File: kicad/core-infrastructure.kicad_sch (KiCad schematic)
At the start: 10 parts, among them J1 JST XH Balance Lead, J2 T-Connector Deans 14 AWG, J3 JST XH Balance Lead, SW2 Latching Push Button, U5 PCA9685PW, U6 JZK 2S 7.4V 8A BMS, U7 MP1584 Buck Converter 5V, U8 ESP32-S3 Super Mini

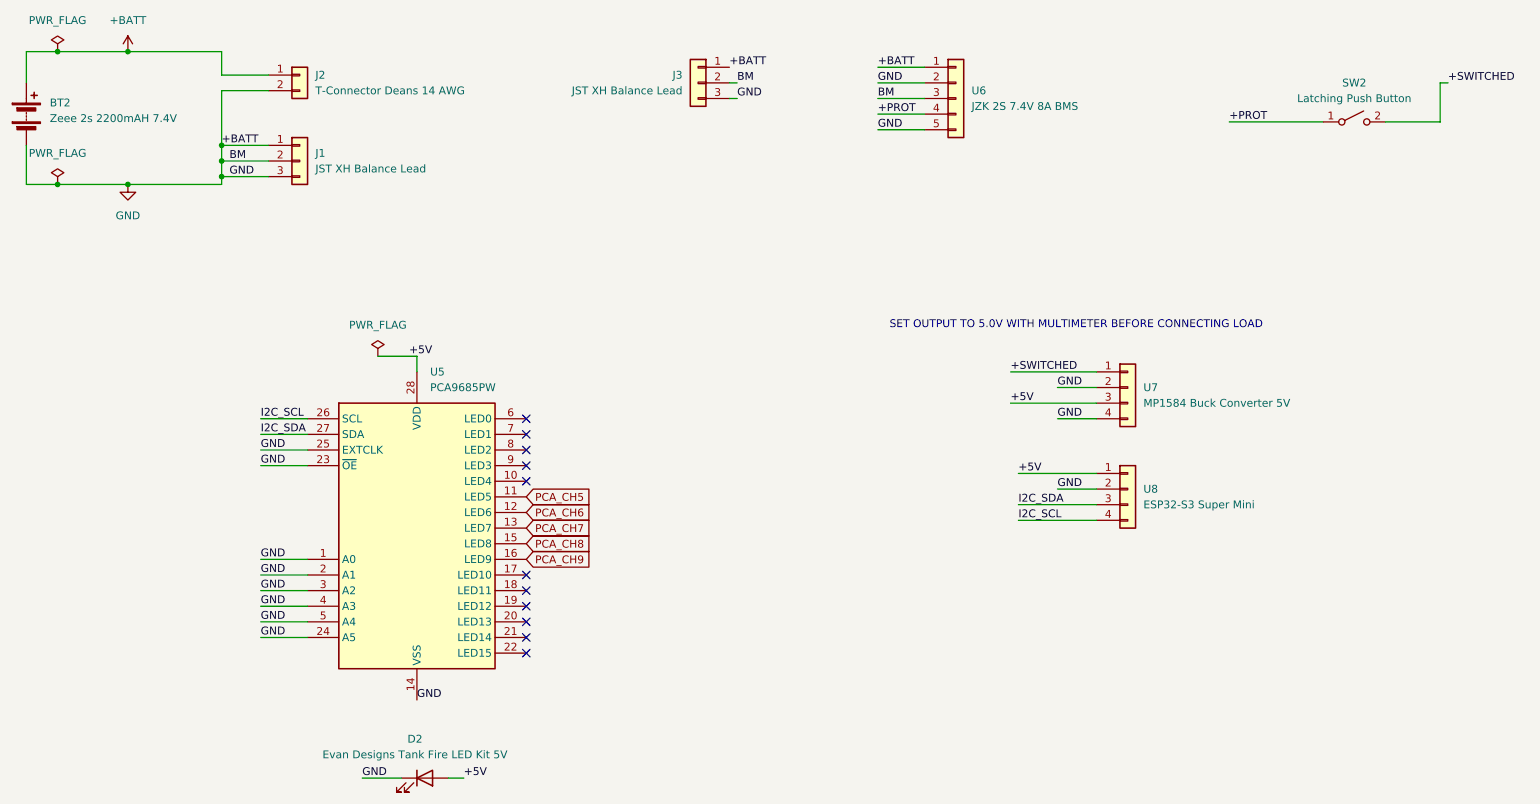
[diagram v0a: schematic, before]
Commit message: docs: remove BMS references from all docs and update schematic
Removes stale BMS component, net labels, and power chain diagram from
schematic-progress.md; updates torso.md, core-infrastructure.md, and
CLAUDE.md to reflect the simplified power chain (lipo → switch → buck →
5V bus). Also includes the updated KiCad schematic and SVG export.
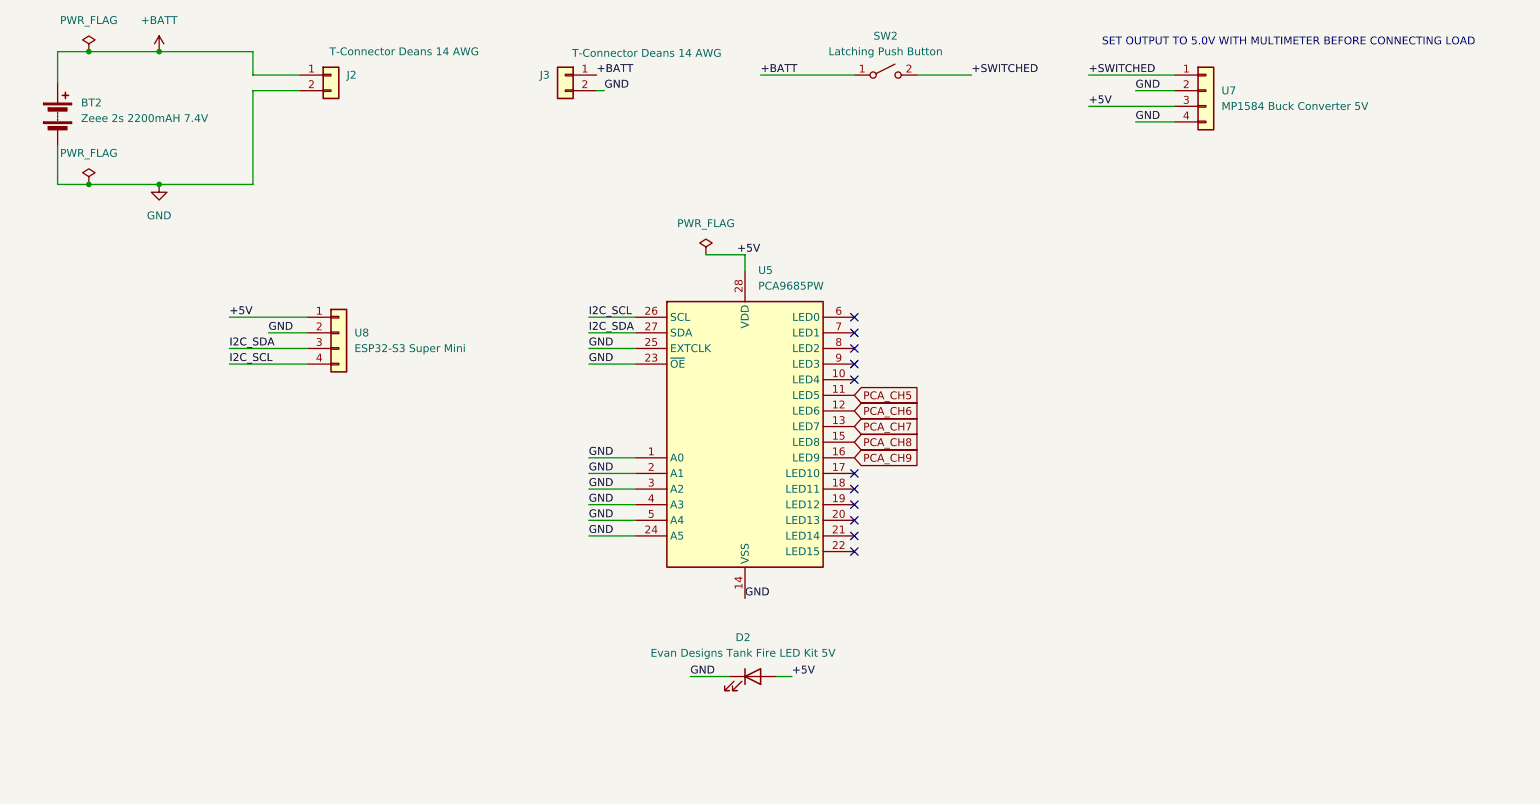
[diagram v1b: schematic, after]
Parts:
- removed J1, J3: JST XH Balance Lead, symbol Connector_Generic:Conn_01x03
- removed U6: JZK 2S 7.4V 8A BMS, symbol Connector_Generic:Conn_01x05
- added J3: T-Connector Deans 14 AWG, symbol Connector_Generic:Conn_01x02
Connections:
- net +PROT is gone; now on net +BATT: SW2.1 (A)
- net +BATT: now also J3.1 (Pin_1); no longer BT2.2 (-), D2.1 (K), J2.2 (Pin_2), U5.1 (A0), U5.14 (VSS), U5.2 (A1), U5.23 (~{OE}), U5.24 (A5), U5.25 (EXTCLK), U5.3 (A2), U5.4 (A3), U5.5 (A4), U7.2 (Pin_2), U7.4 (Pin_4), U8.2 (Pin_2)
- new net GND: BT2.2 (-), D2.1 (K), J2.2 (Pin_2), J3.2 (Pin_2), U5.1 (A0), U5.14 (VSS), U5.2 (A1), U5.23 (~{OE}), U5.24 (A5), U5.25 (EXTCLK), U5.3 (A2), U5.4 (A3), U5.5 (A4), U7.2 (Pin_2), U7.4 (Pin_4), U8.2 (Pin_2)
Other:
- moved on the sheet: BT2, D2, J2, SW2, U5, U7, U8
